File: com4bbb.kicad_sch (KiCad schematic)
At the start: 54 parts, among them J101 RS485, J102 PWR, J103 DCF77, P8 BeagleBone_Black_Header, P9 BeagleBone_Black_Header, SW101 Reset, SW102 PWR, U101 SP3485EN, U102 R-78K5.0-0.5, U103 AT24C512C-SSHD-T, U104 ATECC608A-MAHDA, U105 DS3231MZ

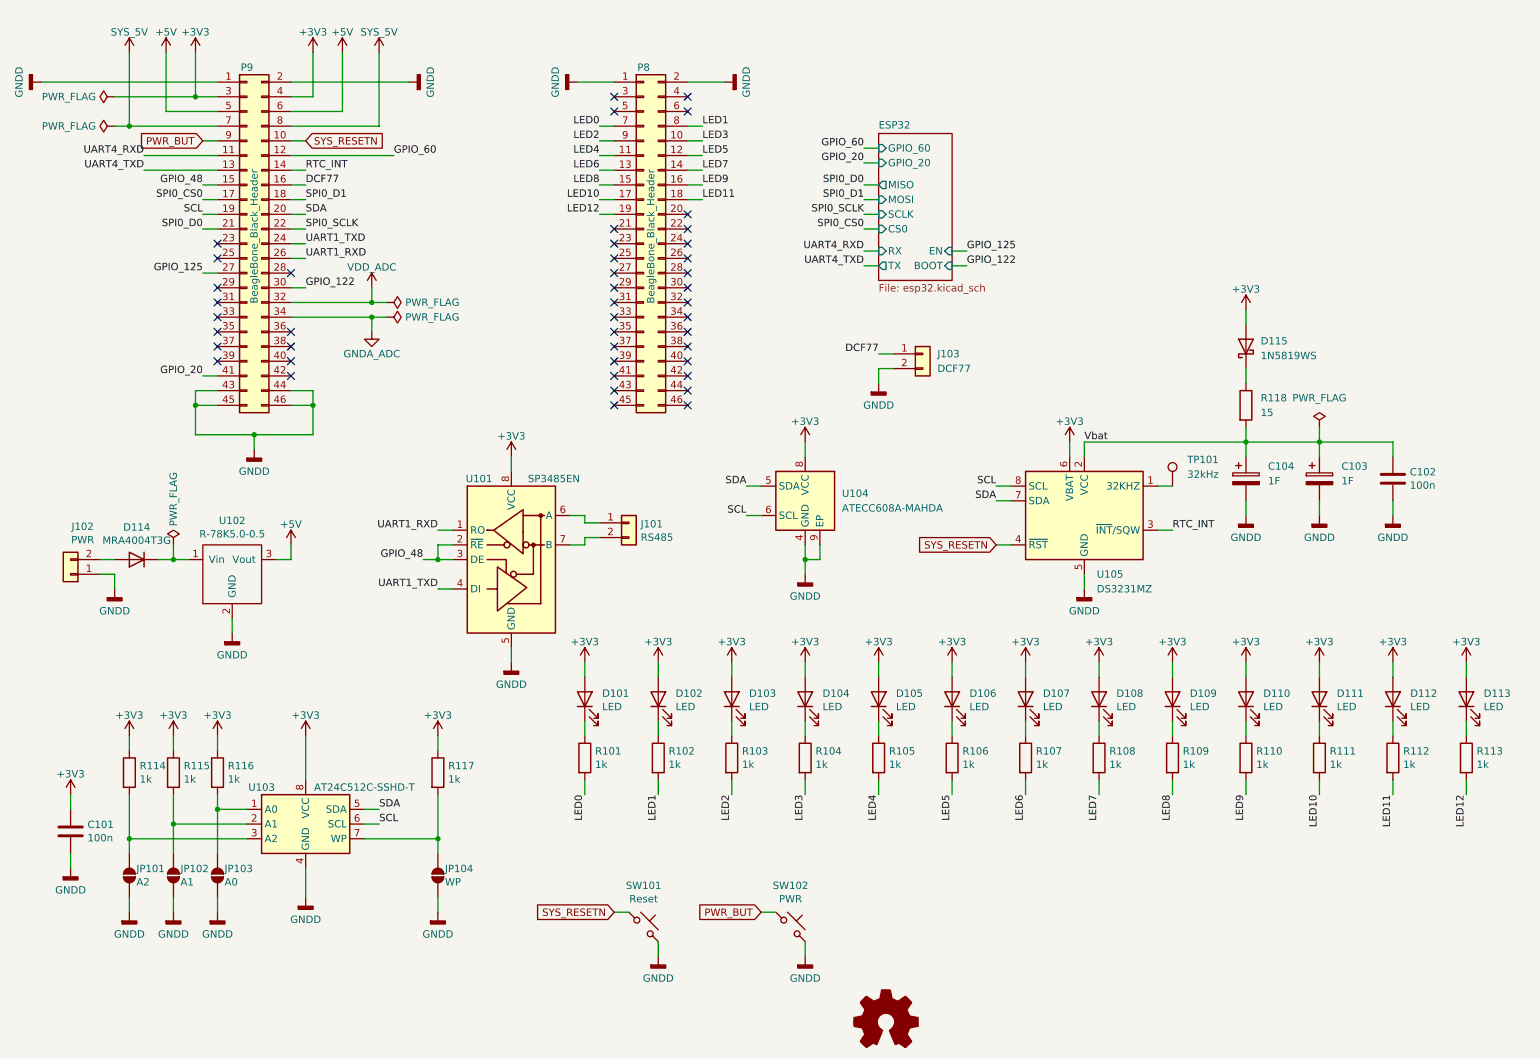
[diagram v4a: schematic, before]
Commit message: Add PPS input
Signed-off-by: Benedikt Spranger <b.spranger@linutronix.de>
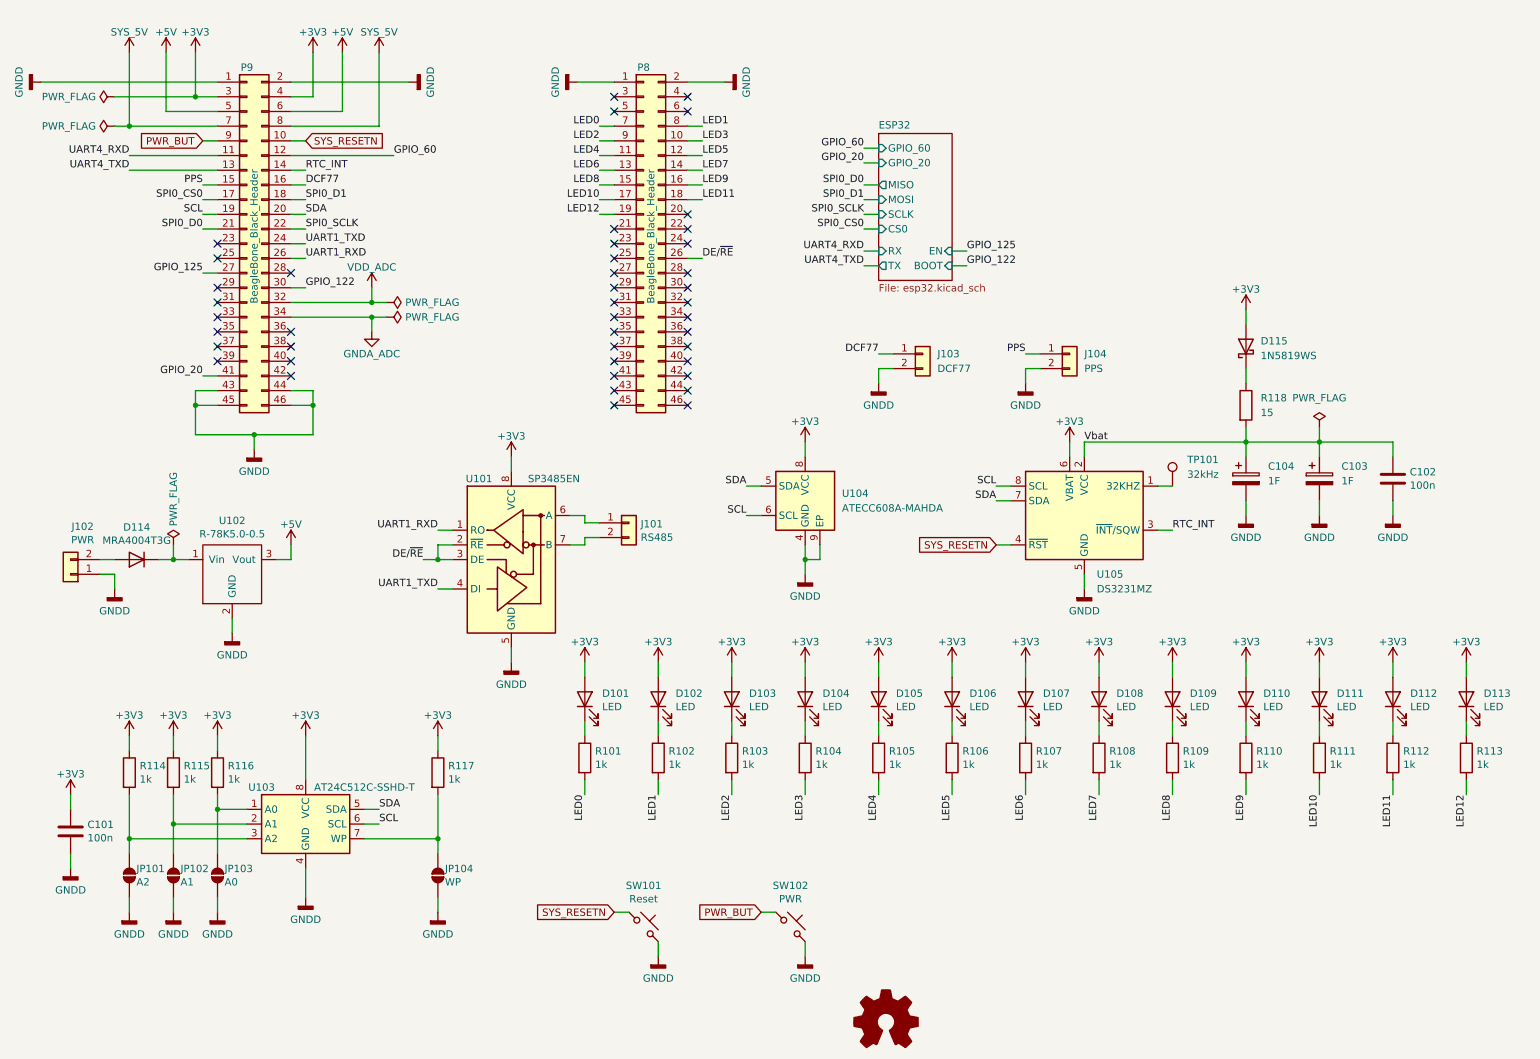
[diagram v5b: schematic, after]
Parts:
- added J104: PPS, Connector_PinHeader_2.54mm:PinHeader_1x02_P2.54mm_Vertical, symbol Connector_Generic:Conn_01x02
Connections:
- net GNDD: now also J104.2 (Pin_2)
- net DE/~{RE}: now reaches P8.26 (Pin_26)
- net DE/~{RE}: now also U101.2 (~{RE}), U101.3 (DE)
- removed net GPIO_48: P9.15 (Pin_15), U101.2 (~{RE}), U101.3 (DE)
- new net PPS: J104.1 (Pin_1), P9.15 (Pin_15)
- no-connect marks 44 -> 43
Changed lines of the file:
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@@
 	)
 	(no_connect
-		(at 132.08 59.69)
-	)
-	(no_connect
 		(at 50.8 64.77)
 	)
@@
 	(wire
 		(pts
+			(xy 193.04 78.74) (xy 190.5 78.74)
+		)
+		(stroke
+			(width 0)
+			(type default)
+		)
+	)
+	(wire
+		(pts
 			(xy 215.9 139.7) (xy 215.9 142.24)
 		)
@@
 	(wire
 		(pts
-			(xy 38.1 41.91) (xy 50.8 41.91)
+			(xy 35.56 41.91) (xy 50.8 41.91)
 		)
 		(stroke
@@
 	(wire
 		(pts
-			(xy 38.1 44.45) (xy 50.8 44.45)
+			(xy 35.56 44.45) (xy 50.8 44.45)
 		)
 		(stroke
@@
 	(wire
 		(pts
+			(xy 132.08 59.69) (xy 134.62 59.69)
+		)
+		(stroke
+			(width 0)
+			(type default)
+		)
+	)
+	(wire
+		(pts
 			(xy 152.4 177.8) (xy 152.4 180.34)
 		)
@@
 	(wire
 		(pts
+			(xy 190.5 78.74) (xy 190.5 81.28)
+		)
+		(stroke
+			(width 0)
+			(type default)
+		)
+	)
+	(wire
+		(pts
 			(xy 63.5 41.91) (xy 81.28 41.91)
 		)
@@
 	(wire
 		(pts
+			(xy 190.5 76.2) (xy 193.04 76.2)
+		)
+		(stroke
+			(width 0)
+			(type default)
+		)
+	)
+	(wire
+		(pts
 			(xy 152.4 149.86) (xy 152.4 152.4)
 		)
@@
 		)
 	)
+	(label "PPS"
+		(at 190.5 76.2 180)
+		(effects
+			(font
+				(size 1.27 1.27)
+			)
+			(justify right bottom)
+		)
+	)
 	(label "LED4"
 		(at 116.84 41.91 180)
@@
 	)
 	(label "UART4_TXD"
-		(at 38.1 44.45 180)
+		(at 35.56 44.45 180)
 		(effects
 			(font
@@
 		)
 	)
+	(label "PPS"
+		(at 48.26 46.99 180)
+		(effects
+			(font
+				(size 1.27 1.27)
+			)
+			(justify right bottom)
+		)
+	)
 	(label "GPIO_122"
 		(at 180.34 60.96 0)
@@
 		)
 	)
-	(label "GPIO_48"
-		(at 48.26 46.99 180)
+	(label "DE{slash}~{RE}"
+		(at 134.62 59.69 0)
 		(effects
 			(font
 				(size 1.27 1.27)
 			)
-			(justify right bottom)
+			(justify left bottom)
 		)
 	)
@@
 	)
 	(label "UART4_RXD"
-		(at 38.1 41.91 180)
+		(at 35.56 41.91 180)
 		(effects
 			(font
@@
 		)
 	)
-	(label "GPIO_48"
-		(at 86.36 111.76 180)
-		(effects
-			(font
-				(size 1.27 1.27)
-			)
-			(justify right bottom)
-		)
-	)
 	(label "LED6"
 		(at 116.84 44.45 180)
@@
 		)
 	)
+	(label "DE{slash}~{RE}"
+		(at 86.36 111.76 180)
+		(effects
+			(font
+				(size 1.27 1.27)
+			)
+			(justify right bottom)
+		)
+	)
 	(label "SCL"
 		(at 142.24 104.14 180)
@@
 	)
 	(symbol
+		(lib_id "Connector_Generic:Conn_01x02")
+		(at 198.12 76.2 0)
+		(unit 1)
+		(exclude_from_sim no)
+		(in_bom yes)
+		(on_board yes)
+		(dnp no)
+		(fields_autoplaced yes)
+		(property "Reference" "J104"
+			(at 200.66 76.1999 0)
+			(effects
+				(font
+					(size 1.27 1.27)
+				)
+				(justify left)
+			)
+		)
+		(property "Value" "PPS"
+			(at 200.66 78.7399 0)
+			(effects
+				(font
+					(size 1.27 1.27)
+				)
+				(justify left)
+			)
+		)
+		(property "Footprint" "Connector_PinHeader_2.54mm:PinHeader_1x02_P2.54mm_Vertical"
+			(at 198.12 76.2 0)
+			(effects
+				(font
+					(size 1.27 1.27)
+				)
+				(hide yes)
+			)
+		)
+		(property "Datasheet" "~"
+			(at 198.12 76.2 0)
+			(effects
+				(font
+					(size 1.27 1.27)
+				)
+				(hide yes)
+			)
+		)
+		(property "Description" "Generic connector, single row, 01x02, script generated (kicad-library-utils/schlib/autogen/connector/)"
+			(at 198.12 76.2 0)
+			(effects
+				(font
+					(size 1.27 1.27)
+				)
+				(hide yes)
+			)
+		)
+		(pin "2"
+		)
+		(pin "1"
+		)
+		(instances
+			(project "com4bbb"
+				(path "/bfd666b6-a268-42c4-a4e5-052a7c5965f6"
+					(reference "J104")
+					(unit 1)
+				)
+			)
+		)
+	)
+	(symbol
 		(lib_id "power:GNDD")
 		(at 254 104.14 0)
@@
 					(unit 1)
 				)
+			)
+		)
+	)
+	(symbol
+		(lib_id "power:GNDD")
+		(at 190.5 81.28 0)
+		(unit 1)
+		(exclude_from_sim no)
+		(in_bom yes)
+		(on_board yes)
+		(dnp no)
+		(property "Reference" "#PWR0155"
+			(at 190.5 87.63 0)
+			(effects
+				(font
+					(size 1.27 1.27)
+				)
+				(hide yes)
+			)
+		)
+		(property "Value" "GNDD"
+			(at 190.5 85.09 0)
+			(effects
+				(font
+					(size 1.27 1.27)
+				)
+			)
+		)
+		(property "Footprint" ""
+			(at 190.5 81.28 0)
+			(effects
+				(font
+					(size 1.524 1.524)
+				)
+				(hide yes)
+			)
+		)
+		(property "Datasheet" ""
+			(at 190.5 81.28 0)
+			(effects
+				(font
+					(size 1.524 1.524)
+				)
+				(hide yes)
+			)
+		)
+		(property "Description" "Power symbol creates a global label with name \"GNDD\" , digital ground"
+			(at 190.5 81.28 0)
+			(effects
+				(font
+					(size 1.27 1.27)
+				)
+				(hide yes)
+			)
+		)
+		(pin "1"
+		)
+		(instances
+			(project "com4bbb"
+				(path "/bfd666b6-a268-42c4-a4e5-052a7c5965f6"
+					(reference "#PWR0155")
+					(unit 1)
+				)
